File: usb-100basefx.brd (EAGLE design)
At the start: 44 x 44 mm, 57 parts, among them IC2 93LC66SN, U1 AX88772B, U2 AFBR-5803Z, U3 MICxxxx, Y1 25MHz

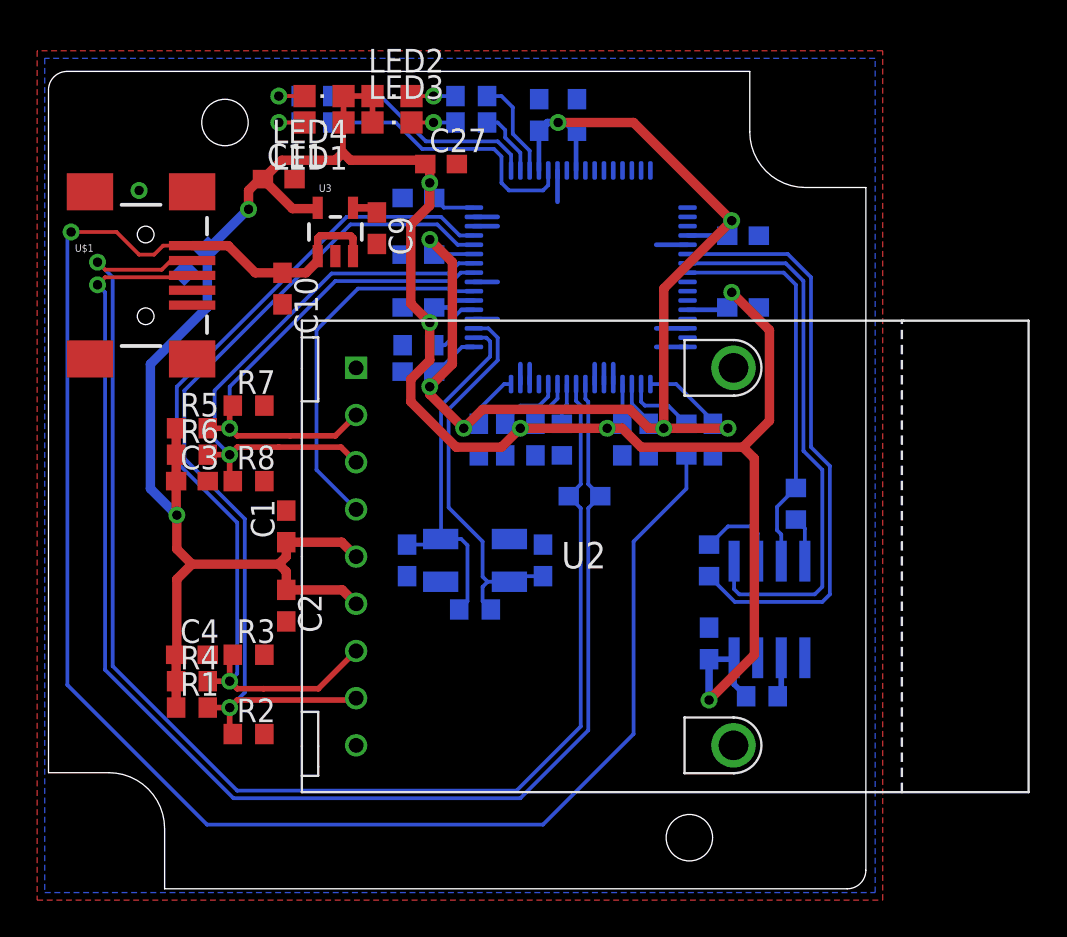
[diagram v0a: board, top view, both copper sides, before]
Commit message: hw: use ld1117 for power
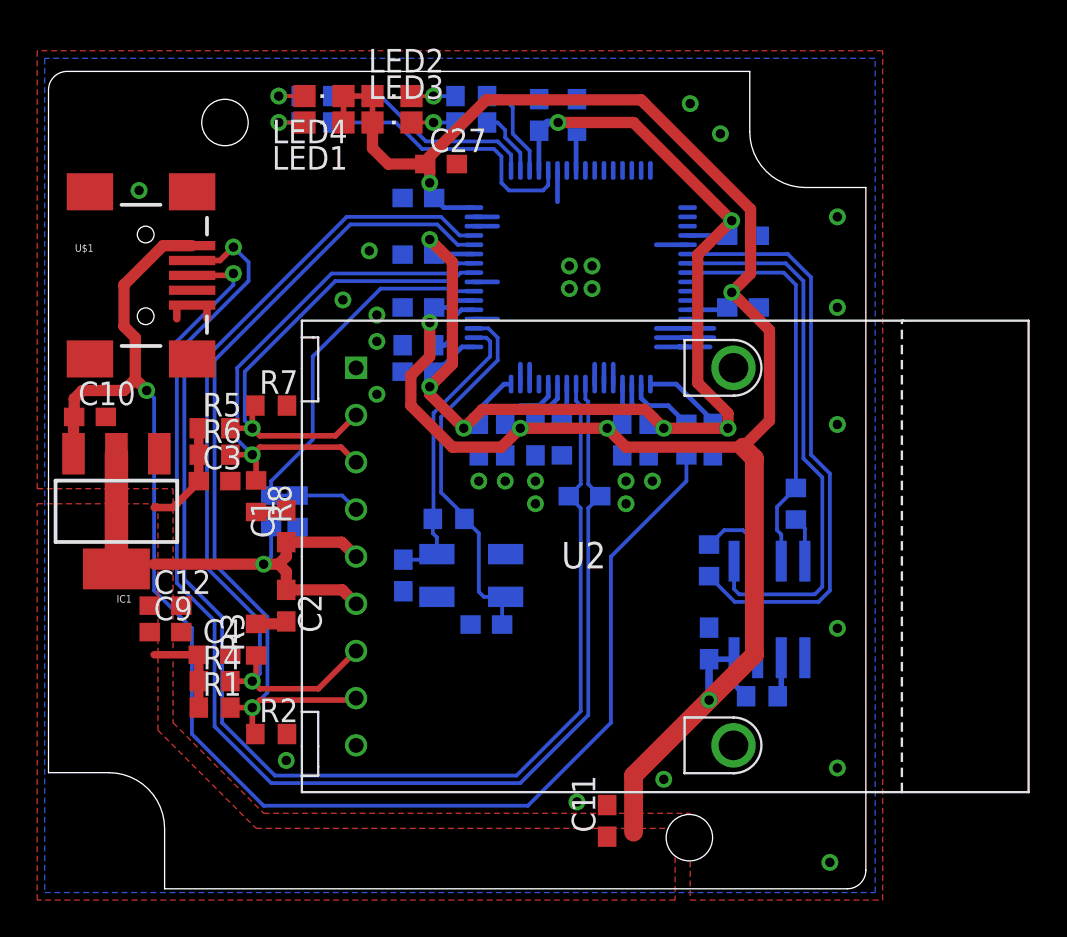
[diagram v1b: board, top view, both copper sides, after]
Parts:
- removed U3: MICxxxx, SparkFun-PowerIC:SOT23-5
- added IC1: LD33, SparkFun-PowerIC:SOT223
- added R20: 130, rcl:R0603
- added R21: 82, rcl:R0603
- moved C11 38.8 mm to (30.1, 3.66), turned to 90 degrees
- moved C9 24.5 mm to (6.30, 13.8), turned to 0 degrees
- moved C12 18.6 mm to (6.30, 15.2), flipped to the top, turned to 0 degrees
- moved C10 12.5 mm to (2.24, 25.4), turned to 0 degrees
- moved R15 5.08 mm to (21.5, 19.9)
- moved C8 4.61 mm to (23.6, 14.2), turned to 0 degrees
- moved C3 1.22 mm to (8.94, 21.9)
- moved C4 1.22 mm to (8.94, 12.6)
- moved R1 1.22 mm to (8.94, 9.75)
- moved R4 1.22 mm to (8.94, 11.2)
- moved R5 1.22 mm to (8.94, 24.8)
- moved R6 1.22 mm to (8.94, 23.4)
- moved R2 1.22 mm to (12.0, 8.33)
- moved R7 1.22 mm to (12.0, 26.0)
- moved R3 0.91 mm to (11.2, 13.4), turned to 90 degrees
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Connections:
- removed net N$6: C9.1, U3.4
- net GND: now also IC1.1, R21.2; no longer U3.2
- net SD: now also R20.2, R21.1
- net USB_VIN: now also IC1.3; no longer U3.1, U3.3
- net VCC: now also C9.1, IC1.2, IC1.4, R20.1; no longer U3.5
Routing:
- net USB_VIN: track 95.3 -> 79.0 mm
- net GND: track 17.2 -> 30.4 mm, vias 1 -> 28
- net USB_DP: track 75.8 -> 70.1 mm
- net USB_DM: track 76.0 -> 70.9 mm
- net XTAL1: track 20.1 -> 15.7 mm
- net SD: track 20.0 -> 23.5 mm
- net TD_DN: track 48.0 -> 46.0 mm
- net TD_DP: track 48.2 -> 46.1 mm
- net RD_DN: track 30.6 -> 28.8 mm
- net RD_DP: track 27.8 -> 26.4 mm
- net N$6: track 1.39 -> 0.00 mm
- net VCC: track 157.4 -> 158.5 mm, vias 8 -> 7
- net XTAL2: track 21.5 -> 20.4 mm
- net EE_CLK: track 4.67 -> 4.14 mm
- added copper zone on layer 1, net VCC

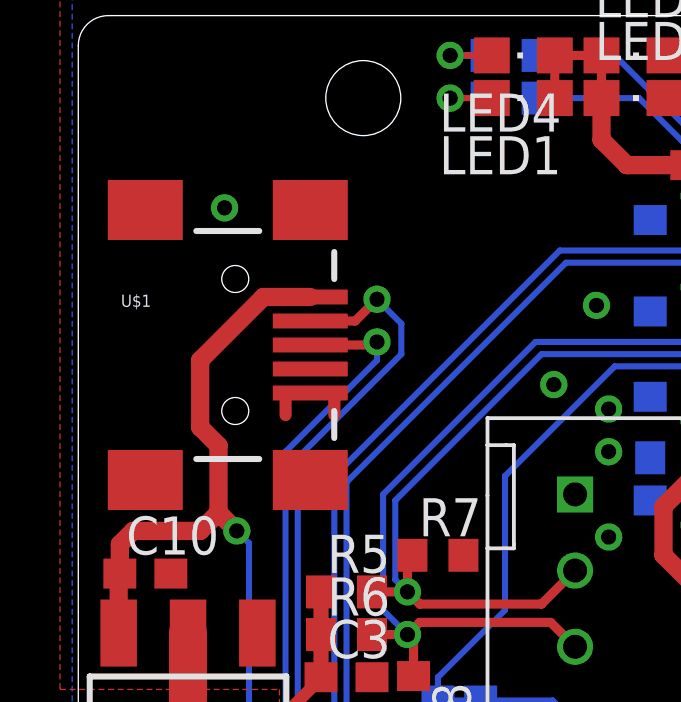
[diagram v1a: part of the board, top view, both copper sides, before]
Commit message: move usb connector
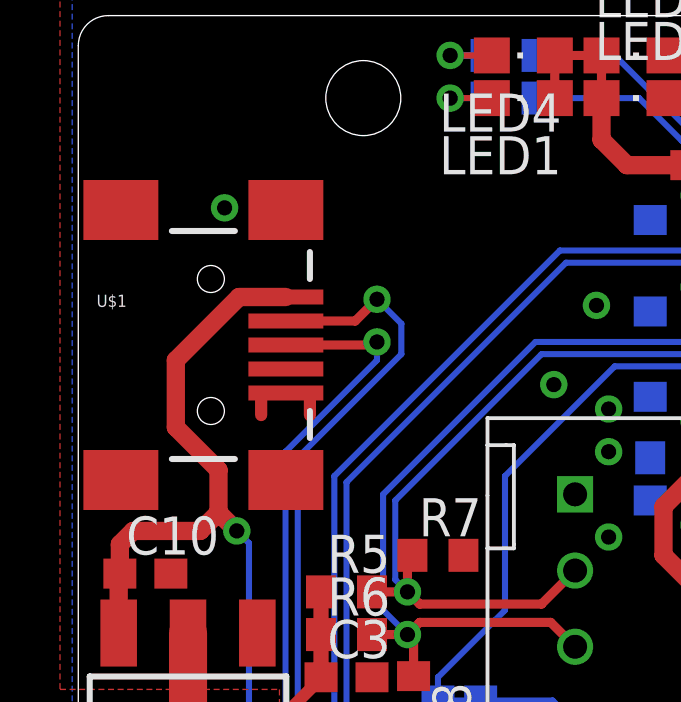
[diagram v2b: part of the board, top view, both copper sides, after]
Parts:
- moved U$1 0.81 mm to (4.42, 33.0)
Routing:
- net USB_DP: track 70.1 -> 70.9 mm
- net USB_DM: track 70.9 -> 71.7 mm
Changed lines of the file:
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@@
 <element name="R1" library="rcl" package="R0603" value="130" x="8.9408" y="9.7536"/>
 <element name="LED1" library="led" package="CHIPLED_0805" value="" x="14.8336" y="41.2496" rot="R90"/>
-<element name="U$1" library="SparkFun-Connectors" package="USB-MINIB" value="USB-MINIB-5PIN" x="5.2324" y="33.02"/>
+<element name="U$1" library="SparkFun-Connectors" package="USB-MINIB" value="USB-MINIB-5PIN" x="4.4196" y="33.02"/>
 <element name="U1" library="balto" package="LQFP64" value="AX88772B" x="28.6512" y="32.9184" rot="MR90"/>
 <element name="U2" library="balto" package="AFBR-5803Z" value="AFBR-5803Z" x="33.3248" y="17.8816"/>
@@
 <via x="33.1216" y="5.8928" extent="1-16" drill="0.508"/>
 <via x="28.448" y="4.6736" extent="1-16" drill="0.508"/>
-<wire x1="7.7324" y1="31.42" x2="8.5344" y2="31.42" width="0.4064" layer="1"/>
-<wire x1="8.5344" y1="31.42" x2="8.5344" y2="30.6832" width="0.4064" layer="1"/>
-<wire x1="7.7324" y1="31.42" x2="6.9088" y2="31.42" width="0.4064" layer="1"/>
-<wire x1="6.9088" y1="31.42" x2="6.9088" y2="30.6832" width="0.4064" layer="1"/>
+<wire x1="6.9196" y1="31.42" x2="7.7216" y2="31.42" width="0.4064" layer="1"/>
+<wire x1="7.7216" y1="31.42" x2="7.7216" y2="30.6832" width="0.4064" layer="1"/>
+<wire x1="6.9196" y1="31.42" x2="6.096" y2="31.42" width="0.4064" layer="1"/>
+<wire x1="6.096" y1="31.42" x2="6.096" y2="30.6832" width="0.4064" layer="1"/>
 <via x="23.1648" y="21.9456" extent="1-16" drill="0.508"/>
 <via x="24.5872" y="21.9456" extent="1-16" drill="0.508"/>
@@
 <wire x1="7.3152" y1="16.6624" x2="9.3472" y2="14.6304" width="0.2032" layer="16"/>
 <wire x1="9.3472" y1="14.6304" x2="9.3472" y2="8.9408" width="0.2032" layer="16"/>
-<wire x1="7.7324" y1="33.82" x2="9.2328" y2="33.82" width="0.3048" layer="1"/>
+<wire x1="6.9196" y1="33.82" x2="9.2328" y2="33.82" width="0.3048" layer="1"/>
 <wire x1="9.2328" y1="33.82" x2="9.9568" y2="34.544" width="0.3048" layer="1"/>
 <wire x1="9.9568" y1="34.544" x2="10.7696" y2="33.7312" width="0.2032" layer="16"/>
@@
 <wire x1="29.0576" y1="9.3472" x2="29.0576" y2="20.486" width="0.2032" layer="16"/>
 <wire x1="11.9888" y1="5.6896" x2="25.4" y2="5.6896" width="0.2032" layer="16"/>
-<wire x1="7.7324" y1="33.02" x2="9.8552" y2="33.02" width="0.3048" layer="1"/>
+<wire x1="6.9196" y1="33.02" x2="9.8552" y2="33.02" width="0.3048" layer="1"/>
 <wire x1="9.8552" y1="33.02" x2="9.9568" y2="33.1216" width="0.3048" layer="1"/>
 <wire x1="9.9568" y1="33.1216" x2="9.9568" y2="32.512" width="0.2032" layer="16"/>
@@
 <contactref element="C10" pad="1"/>
 <contactref element="IC1" pad="3"/>
-<wire x1="7.7324" y1="34.62" x2="6.172" y2="34.62" width="0.6096" layer="1"/>
-<wire x1="6.172" y1="34.62" x2="4.064" y2="32.512" width="0.6096" layer="1"/>
+<wire x1="6.9196" y1="34.62" x2="5.3592" y2="34.62" width="0.6096" layer="1"/>
+<wire x1="5.3592" y1="34.62" x2="3.2512" y2="32.512" width="0.6096" layer="1"/>
 <wire x1="4.064" y1="26.8224" x2="1.8288" y2="26.8224" width="0.6096" layer="1"/>
 <wire x1="1.8288" y1="26.8224" x2="1.3852" y2="26.3788" width="0.6096" layer="1"/>
 <wire x1="1.3852" y1="25.4" x2="1.3852" y2="26.3788" width="0.6096" layer="1"/>
-<wire x1="4.064" y1="32.512" x2="4.064" y2="30.2768" width="0.6096" layer="1"/>
-<wire x1="4.064" y1="30.2768" x2="4.6736" y2="29.6672" width="0.6096" layer="1"/>
+<wire x1="3.2512" y1="32.512" x2="3.2512" y2="30.2768" width="0.6096" layer="1"/>
+<wire x1="3.2512" y1="30.2768" x2="4.6736" y2="28.8544" width="0.6096" layer="1"/>
 <wire x1="1.3462" y1="23.4188" x2="1.3462" y2="25.361" width="0.6096" layer="1"/>
 <wire x1="1.3462" y1="25.361" x2="1.3852" y2="25.4" width="0.6096" layer="1"/>
@@
 <wire x1="4.064" y1="26.8224" x2="4.6736" y2="27.432" width="0.6096" layer="1"/>
 <wire x1="4.6736" y1="27.432" x2="5.2832" y2="26.8224" width="0.6096" layer="1"/>
-<wire x1="4.6736" y1="29.6672" x2="4.6736" y2="27.432" width="0.6096" layer="1"/>
+<wire x1="4.6736" y1="28.8544" x2="4.6736" y2="27.432" width="0.6096" layer="1"/>
 <wire x1="5.6896" y1="26.416" x2="5.2832" y2="26.8224" width="0.2032" layer="16"/>
 </signal>
